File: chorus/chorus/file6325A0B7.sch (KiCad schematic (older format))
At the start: 6 parts, among them U2 TL074

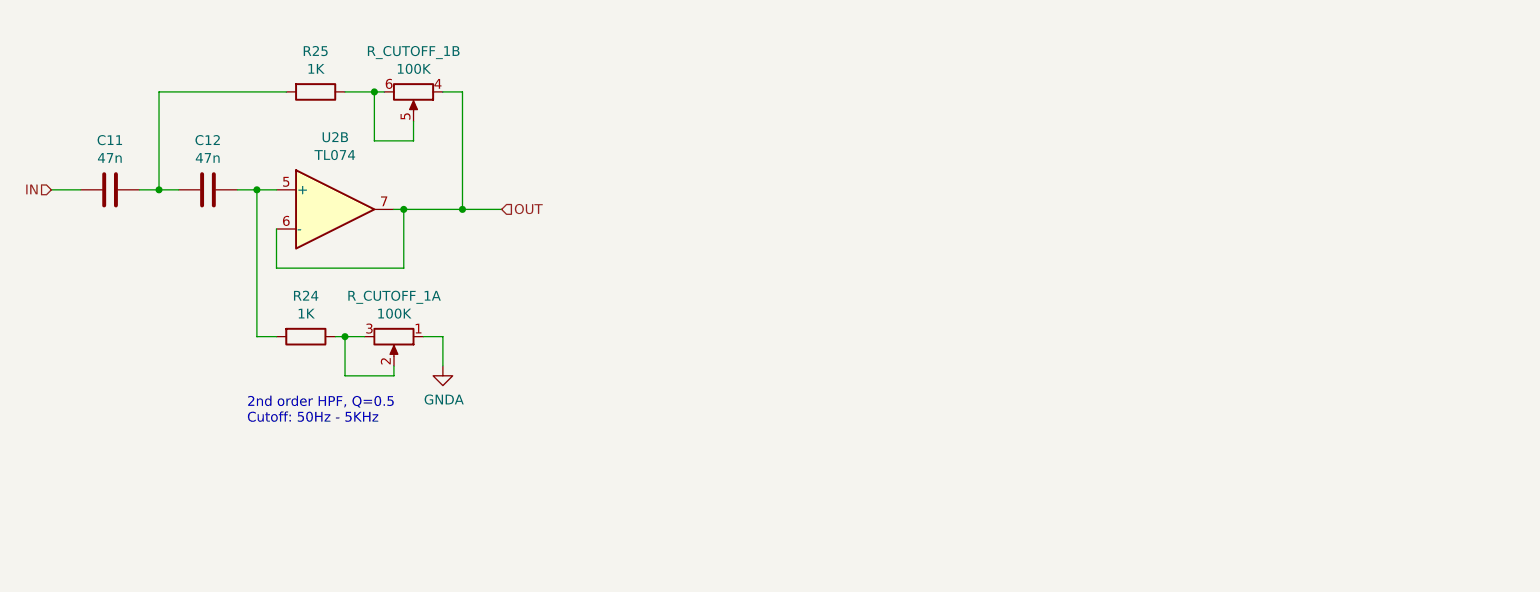
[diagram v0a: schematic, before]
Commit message: add wet/dry mix and recalculate filters
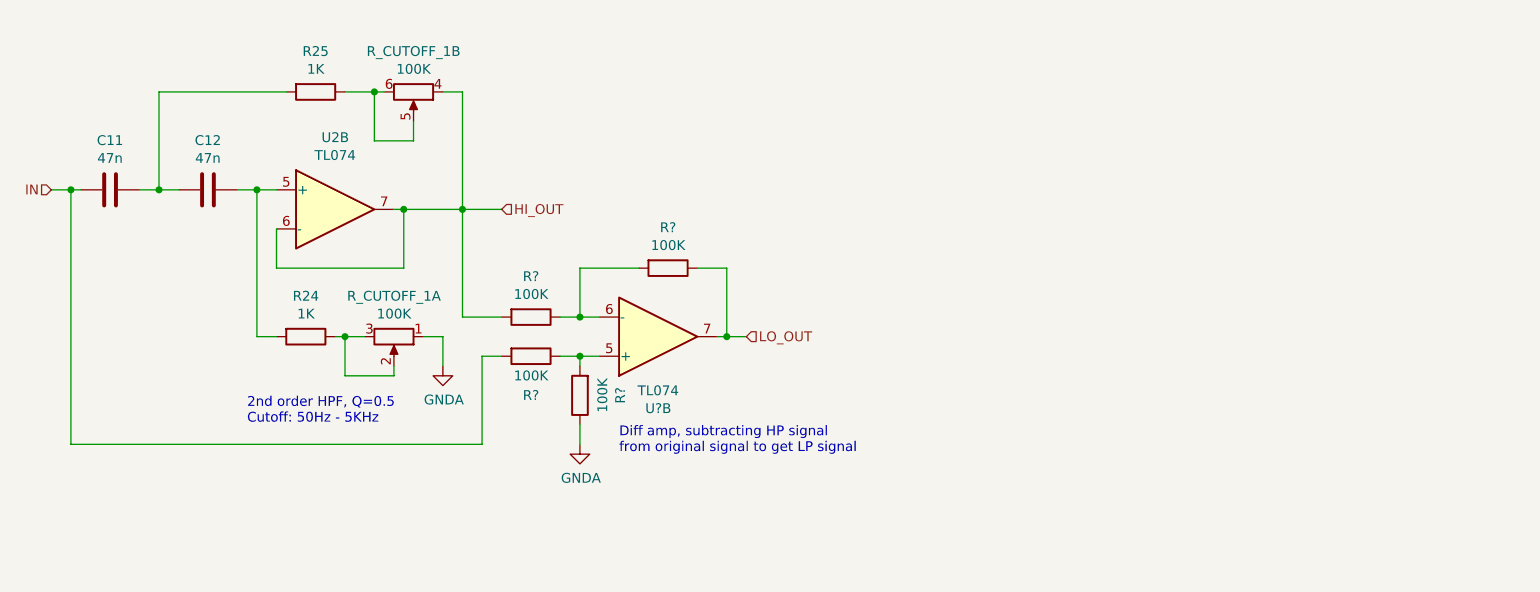
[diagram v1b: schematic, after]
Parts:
- added R? (x4): 100K, Resistor_THT:R_Axial_DIN0204_L3.6mm_D1.6mm_P2.54mm_Vertical, symbol Device:R
- added U?: TL074, Package_DIP:DIP-14_W7.62mm, symbol Amplifier_Operational:TL074
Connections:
- net GNDA: now also R?.1
- net IN: now also R?.2
- net OUT renamed HI_OUT
- net HI_OUT: now also R?.2
- new net: R?.1, R?.2, U?.5 (+)
- new net: R?.1, R?.2, U?.6 (-)
- new net LO_OUT: R?.1, U?.7
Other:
- note added: "Diff amp, subtracting HP signal\nfrom original signal to get LP signal"
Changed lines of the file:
@@
 $Descr A4 11693 8268
 encoding utf-8
-Sheet 6 6
+Sheet 5 6
 Title ""
 Date ""
@@
 IN
 Wire Wire Line
-	4000 3600 4150 3600
+	4000 3600 4100 3600
 Text HLabel 6300 3700 2    50   Input ~ 0
-OUT
+HI_OUT
+Text HLabel 7550 4350 2    50   Input ~ 0
+LO_OUT
+$Comp
+L Amplifier_Operational:TL074 U?
+U 2 1 62A49A72
+P 7100 4350
+AR Path="/62A49A72" Ref="U?"  Part="2"
+AR Path="/6325A0B8/62A49A72" Ref="U?"  Part="2"
+F 0 "U?" H 7100 4717 50  0000 C CNN
+F 1 "TL074" H 7100 4626 50  0000 C CNN
+F 2 "Package_DIP:DIP-14_W7.62mm" H 7050 4450 50  0001 C CNN
+F 3 "http://www.ti.com/lit/ds/symlink/tl071.pdf" H 7150 4550 50  0001 C CNN
+	2    7100 4350
+	1    0    0    1
+$EndComp
+Text Notes 6900 4950 0    50   ~ 0
+Diff amp, subtracting HP signal\nfrom original signal to get LP signal
+$Comp
+L Device:R R?
+U 1 1 62A50D45
+P 6450 4450
+AR Path="/62A50D45" Ref="R?"  Part="1"
+AR Path="/6325A0B8/62A50D45" Ref="R?"  Part="1"
+F 0 "R?" V 6650 4450 50  0000 C CNN
+F 1 "100K" V 6550 4450 50  0000 C CNN
+F 2 "Resistor_THT:R_Axial_DIN0204_L3.6mm_D1.6mm_P2.54mm_Vertical" V 6380 4450 50  0001 C CNN
+F 3 "~" H 6450 4450 50  0001 C CNN
+	1    6450 4450
+	0    1    1    0
+$EndComp
+$Comp
+L Device:R R?
+U 1 1 62A52C2B
+P 6450 4250
+AR Path="/62A52C2B" Ref="R?"  Part="1"
+AR Path="/6325A0B8/62A52C2B" Ref="R?"  Part="1"
+F 0 "R?" V 6243 4250 50  0000 C CNN
+F 1 "100K" V 6334 4250 50  0000 C CNN
+F 2 "Resistor_THT:R_Axial_DIN0204_L3.6mm_D1.6mm_P2.54mm_Vertical" V 6380 4250 50  0001 C CNN
+F 3 "~" H 6450 4250 50  0001 C CNN
+	1    6450 4250
+	0    1    1    0
+$EndComp
+$Comp
+L Device:R R?
+U 1 1 62A53369
+P 7150 4000
+AR Path="/62A53369" Ref="R?"  Part="1"
+AR Path="/6325A0B8/62A53369" Ref="R?"  Part="1"
+F 0 "R?" V 6943 4000 50  0000 C CNN
+F 1 "100K" V 7034 4000 50  0000 C CNN
+F 2 "Resistor_THT:R_Axial_DIN0204_L3.6mm_D1.6mm_P2.54mm_Vertical" V 7080 4000 50  0001 C CNN
+F 3 "~" H 7150 4000 50  0001 C CNN
+	1    7150 4000
+	0    1    1    0
+$EndComp
+$Comp
+L Device:R R?
+U 1 1 62A538EE
+P 6700 4650
+AR Path="/62A538EE" Ref="R?"  Part="1"
+AR Path="/6325A0B8/62A538EE" Ref="R?"  Part="1"
+F 0 "R?" V 6493 4650 50  0000 C CNN
+F 1 "100K" V 6584 4650 50  0000 C CNN
+F 2 "Resistor_THT:R_Axial_DIN0204_L3.6mm_D1.6mm_P2.54mm_Vertical" V 6630 4650 50  0001 C CNN
+F 3 "~" H 6700 4650 50  0001 C CNN
+	1    6700 4650
+	-1   0    0    1
+$EndComp
+Wire Wire Line
+	6600 4450 6700 4450
+Wire Wire Line
+	6700 4500 6700 4450
+Connection ~ 6700 4450
+Wire Wire Line
+	6700 4450 6800 4450
+Wire Wire Line
+	6600 4250 6700 4250
+Wire Wire Line
+	7000 4000 6700 4000
+Wire Wire Line
+	6700 4000 6700 4250
+Connection ~ 6700 4250
+Wire Wire Line
+	6700 4250 6800 4250
+Wire Wire Line
+	7400 4350 7450 4350
+Wire Wire Line
+	7450 4350 7450 4000
+Wire Wire Line
+	7450 4000 7300 4000
+Wire Wire Line
+	7550 4350 7450 4350
+Connection ~ 7450 4350
+$Comp
+L power:GNDA #PWR?
+U 1 1 62A57D82
+P 6700 4900
+AR Path="/62A57D82" Ref="#PWR?"  Part="1"
+AR Path="/6325A0B8/62A57D82" Ref="#PWR?"  Part="1"
+F 0 "#PWR?" H 6700 4650 50  0001 C CNN
+F 1 "GNDA" H 6705 4727 50  0000 C CNN
+F 2 "" H 6700 4900 50  0001 C CNN
+F 3 "" H 6700 4900 50  0001 C CNN
+	1    6700 4900
+	1    0    0    -1
+$EndComp
+Wire Wire Line
+	6700 4900 6700 4800
+Wire Wire Line
+	6300 4450 6200 4450
+Wire Wire Line
+	6200 4450 6200 4900
+Wire Wire Line
+	6200 4900 4100 4900
+Wire Wire Line
+	4100 4900 4100 3600
+Connection ~ 4100 3600
+Wire Wire Line
+	4100 3600 4150 3600
+Wire Wire Line
+	6300 4250 6100 4250
+Wire Wire Line
+	6100 4250 6100 3700
 $EndSCHEMATC

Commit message: remove dry/wet, add higher dry frequencies
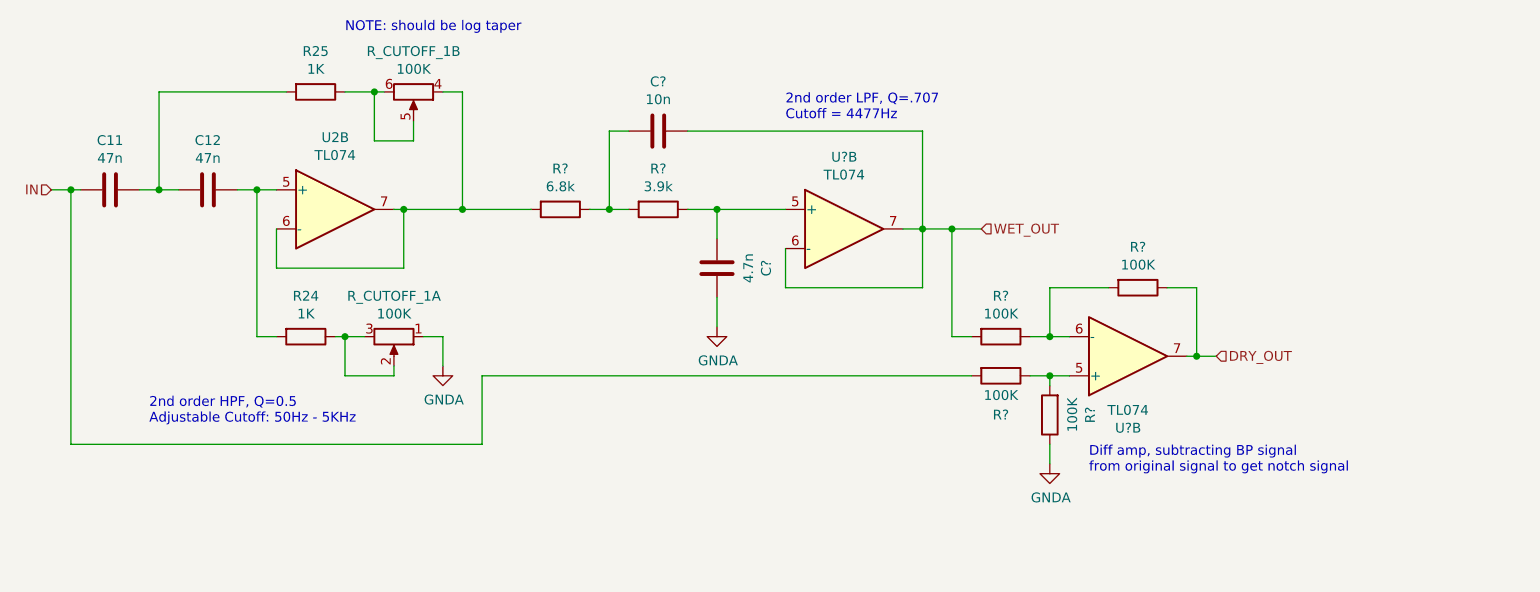
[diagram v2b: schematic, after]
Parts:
- added C?: 10n, Capacitor_THT:C_Disc_D6.0mm_W2.5mm_P5.00mm, symbol Device:C
- added C?: 4.7n, Capacitor_THT:C_Disc_D6.0mm_W2.5mm_P5.00mm, symbol Device:C
- added R?: 6.8k, Resistor_THT:R_Axial_DIN0204_L3.6mm_D1.6mm_P2.54mm_Vertical, symbol Device:R
- added R?: 3.9k, Resistor_THT:R_Axial_DIN0204_L3.6mm_D1.6mm_P2.54mm_Vertical, symbol Device:R
- added U?: TL074, Package_DIP:DIP-14_W7.62mm, symbol Amplifier_Operational:TL074
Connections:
- net GNDA: now also C?.1
- net HI_OUT: no longer names the net of R_CUTOFF_1.4, U2.6 (-), U2.7
- net HI_OUT: now also R?.2; no longer R?.2
- net LO_OUT renamed DRY_OUT
- new net: C?.2, R?.1, U?.5 (+)
- new net: C?.2, R?.1, R?.2
- new net WET_OUT: C?.1, R?.2, U?.6 (-), U?.7
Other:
- note added: "2nd order HPF, Q=0.5\nAdjustable Cutoff: 50Hz - 5KHz"
- note added: "2nd order LPF, Q=.707\nCutoff = 4477Hz"
- note added: "Diff amp, subtracting BP signal\nfrom original signal to get notch signal"
- note added: "NOTE: should be log taper"
- note removed: "2nd order HPF, Q=0.5\nCutoff: 50Hz - 5KHz"
- note removed: "Diff amp, subtracting HP signal\nfrom original signal to get LP signal"
- moved on the sheet: R?, U?B

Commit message: improve BP calculations imperically
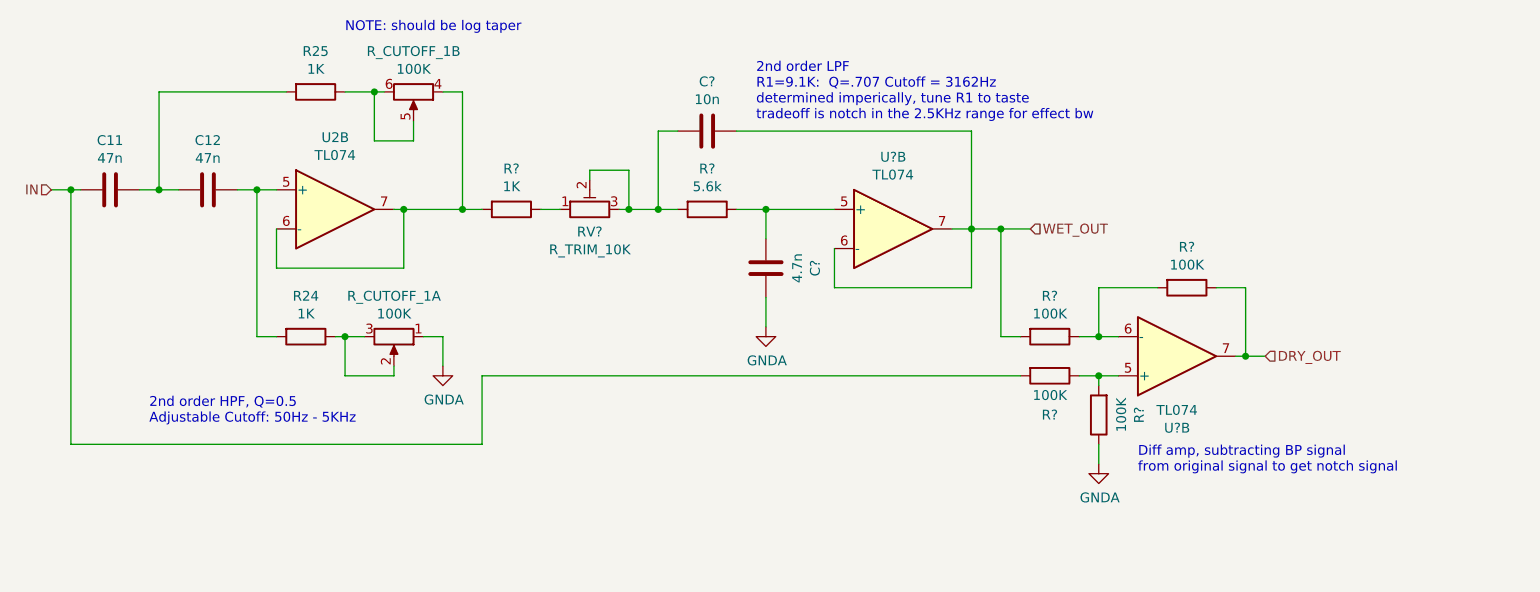
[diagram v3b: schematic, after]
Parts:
- added RV?: R_TRIM_10K, symbol Device:R_POT_TRIM
- R?: value 6.8k -> 1K
- R?: value 3.9k -> 5.6k
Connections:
- net at C?.2, R?.2: now also RV?.2, RV?.3; no longer R?.1
- new net: R?.1, RV?.1
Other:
- note added: "2nd order LPF\nR1=9.1K: Q=.707 Cutoff = 3162Hz\ndetermined imperically, tune R1 to taste\ntradeoff is notch in the 2.5KHz range for effect bw"
- note removed: "2nd order LPF, Q=.707\nCutoff = 4477Hz"
- moved on the sheet: C?, R?, U?B

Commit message: assembled psu and clock
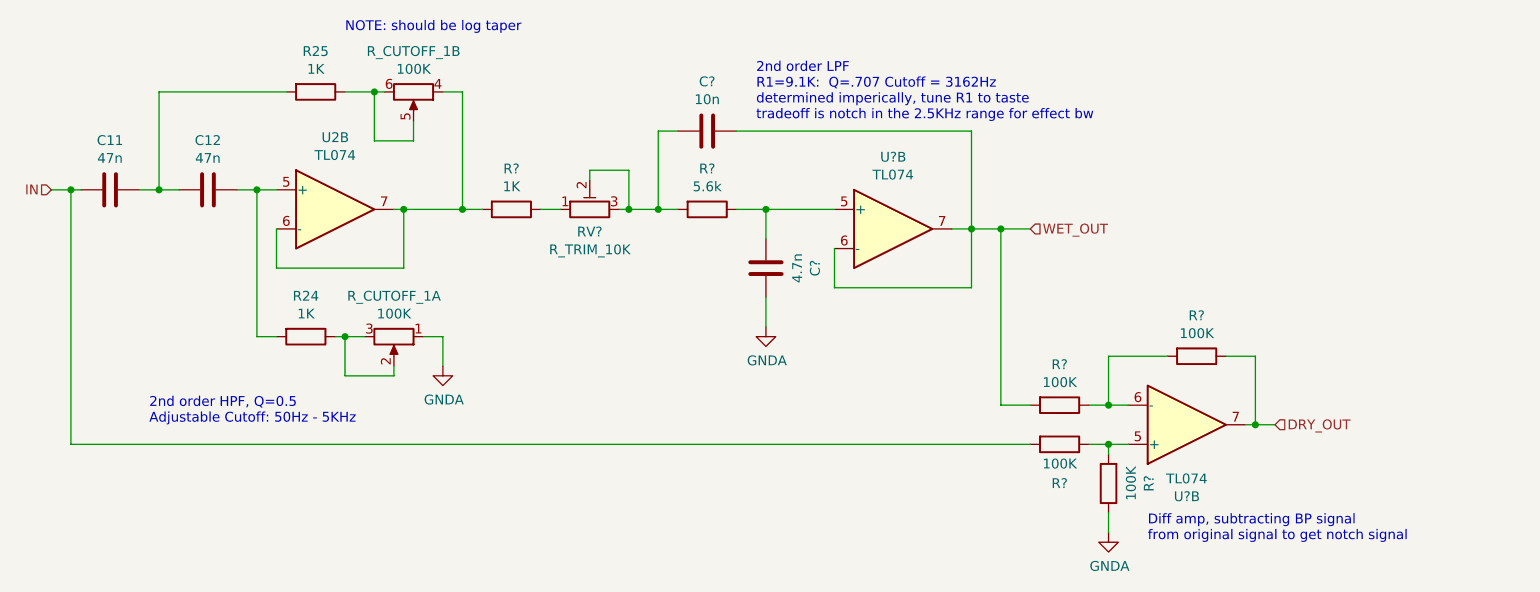
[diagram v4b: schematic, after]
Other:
- moved on the sheet: R?, U?B
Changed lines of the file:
@@
 Text HLabel 9000 3800 2    50   Input ~ 0
 WET_OUT
-Text HLabel 10200 4450 2    50   Input ~ 0
+Text HLabel 10250 4800 2    50   Input ~ 0
 DRY_OUT
 $Comp
 L Amplifier_Operational:TL074 U?
 U 2 1 62A49A72
-P 9750 4450
+P 9800 4800
 AR Path="/62A49A72" Ref="U?"  Part="2"
 AR Path="/6325A0B8/62A49A72" Ref="U?"  Part="2"
-F 0 "U?" H 9750 4817 50  0000 C CNN
-F 1 "TL074" H 9750 4726 50  0000 C CNN
-F 2 "Package_DIP:DIP-14_W7.62mm" H 9700 4550 50  0001 C CNN
-F 3 "http://www.ti.com/lit/ds/symlink/tl071.pdf" H 9800 4650 50  0001 C CNN
-	2    9750 4450
+F 0 "U?" H 9800 5167 50  0000 C CNN
+F 1 "TL074" H 9800 5076 50  0000 C CNN
+F 2 "Package_DIP:DIP-14_W7.62mm" H 9750 4900 50  0001 C CNN
+F 3 "http://www.ti.com/lit/ds/symlink/tl071.pdf" H 9850 5000 50  0001 C CNN
+	2    9800 4800
 	1    0    0    1
 $EndComp
-Text Notes 9550 5050 0    50   ~ 0
+Text Notes 9600 5400 0    50   ~ 0
 Diff amp, subtracting BP signal\nfrom original signal to get notch signal
 $Comp
 L Device:R R?
 U 1 1 62A50D45
-P 9100 4550
+P 9150 4900
 AR Path="/62A50D45" Ref="R?"  Part="1"
 AR Path="/6325A0B8/62A50D45" Ref="R?"  Part="1"
-F 0 "R?" V 9300 4550 50  0000 C CNN
-F 1 "100K" V 9200 4550 50  0000 C CNN
-F 2 "Resistor_THT:R_Axial_DIN0204_L3.6mm_D1.6mm_P2.54mm_Vertical" V 9030 4550 50  0001 C CNN
-F 3 "~" H 9100 4550 50  0001 C CNN
-	1    9100 4550
+F 0 "R?" V 9350 4900 50  0000 C CNN
+F 1 "100K" V 9250 4900 50  0000 C CNN
+F 2 "Resistor_THT:R_Axial_DIN0204_L3.6mm_D1.6mm_P2.54mm_Vertical" V 9080 4900 50  0001 C CNN
+F 3 "~" H 9150 4900 50  0001 C CNN
+	1    9150 4900
 	0    1    1    0
 $EndComp
@@
 L Device:R R?
 U 1 1 62A52C2B
-P 9100 4350
+P 9150 4700
 AR Path="/62A52C2B" Ref="R?"  Part="1"
 AR Path="/6325A0B8/62A52C2B" Ref="R?"  Part="1"
-F 0 "R?" V 8893 4350 50  0000 C CNN
-F 1 "100K" V 8984 4350 50  0000 C CNN
-F 2 "Resistor_THT:R_Axial_DIN0204_L3.6mm_D1.6mm_P2.54mm_Vertical" V 9030 4350 50  0001 C CNN
-F 3 "~" H 9100 4350 50  0001 C CNN
-	1    9100 4350
+F 0 "R?" V 8943 4700 50  0000 C CNN
+F 1 "100K" V 9034 4700 50  0000 C CNN
+F 2 "Resistor_THT:R_Axial_DIN0204_L3.6mm_D1.6mm_P2.54mm_Vertical" V 9080 4700 50  0001 C CNN
+F 3 "~" H 9150 4700 50  0001 C CNN
+	1    9150 4700
 	0    1    1    0
 $EndComp
@@
 L Device:R R?
 U 1 1 62A53369
-P 9800 4100
+P 9850 4450
 AR Path="/62A53369" Ref="R?"  Part="1"
 AR Path="/6325A0B8/62A53369" Ref="R?"  Part="1"
-F 0 "R?" V 9593 4100 50  0000 C CNN
-F 1 "100K" V 9684 4100 50  0000 C CNN
-F 2 "Resistor_THT:R_Axial_DIN0204_L3.6mm_D1.6mm_P2.54mm_Vertical" V 9730 4100 50  0001 C CNN
-F 3 "~" H 9800 4100 50  0001 C CNN
-	1    9800 4100
+F 0 "R?" V 9643 4450 50  0000 C CNN
+F 1 "100K" V 9734 4450 50  0000 C CNN
+F 2 "Resistor_THT:R_Axial_DIN0204_L3.6mm_D1.6mm_P2.54mm_Vertical" V 9780 4450 50  0001 C CNN
+F 3 "~" H 9850 4450 50  0001 C CNN
+	1    9850 4450
 	0    1    1    0
 $EndComp
@@
 L Device:R R?
 U 1 1 62A538EE
-P 9350 4750
+P 9400 5100
 AR Path="/62A538EE" Ref="R?"  Part="1"
 AR Path="/6325A0B8/62A538EE" Ref="R?"  Part="1"
-F 0 "R?" V 9143 4750 50  0000 C CNN
-F 1 "100K" V 9234 4750 50  0000 C CNN
-F 2 "Resistor_THT:R_Axial_DIN0204_L3.6mm_D1.6mm_P2.54mm_Vertical" V 9280 4750 50  0001 C CNN
-F 3 "~" H 9350 4750 50  0001 C CNN
-	1    9350 4750
+F 0 "R?" V 9193 5100 50  0000 C CNN
+F 1 "100K" V 9284 5100 50  0000 C CNN
+F 2 "Resistor_THT:R_Axial_DIN0204_L3.6mm_D1.6mm_P2.54mm_Vertical" V 9330 5100 50  0001 C CNN
+F 3 "~" H 9400 5100 50  0001 C CNN
+	1    9400 5100
 	-1   0    0    1
 $EndComp
 Wire Wire Line
-	9250 4550 9350 4550
-Wire Wire Line
-	9350 4600 9350 4550
-Connection ~ 9350 4550
-Wire Wire Line
-	9350 4550 9450 4550
-Wire Wire Line
-	9250 4350 9350 4350
-Wire Wire Line
-	9650 4100 9350 4100
-Wire Wire Line
-	9350 4100 9350 4350
-Connection ~ 9350 4350
-Wire Wire Line
-	9350 4350 9450 4350
-Wire Wire Line
-	10050 4450 10100 4450
-Wire Wire Line
-	10100 4450 10100 4100
-Wire Wire Line
-	10100 4100 9950 4100
-Wire Wire Line
-	10200 4450 10100 4450
-Connection ~ 10100 4450
+	9300 4900 9400 4900
+Wire Wire Line
+	9400 4950 9400 4900
+Connection ~ 9400 4900
+Wire Wire Line
+	9400 4900 9500 4900
+Wire Wire Line
+	9300 4700 9400 4700
+Wire Wire Line
+	9700 4450 9400 4450
+Wire Wire Line
+	9400 4450 9400 4700
+Connection ~ 9400 4700
+Wire Wire Line
+	9400 4700 9500 4700
+Wire Wire Line
+	10100 4800 10150 4800
+Wire Wire Line
+	10150 4800 10150 4450
+Wire Wire Line
+	10150 4450 10000 4450
+Wire Wire Line
+	10250 4800 10150 4800
+Connection ~ 10150 4800
 $Comp
 L power:GNDA #PWR?
 U 1 1 62A57D82
-P 9350 5000
+P 9400 5350
 AR Path="/62A57D82" Ref="#PWR?"  Part="1"
 AR Path="/6325A0B8/62A57D82" Ref="#PWR?"  Part="1"
-F 0 "#PWR?" H 9350 4750 50  0001 C CNN
-F 1 "GNDA" H 9355 4827 50  0000 C CNN
-F 2 "" H 9350 5000 50  0001 C CNN
-F 3 "" H 9350 5000 50  0001 C CNN
-	1    9350 5000
+F 0 "#PWR?" H 9400 5100 50  0001 C CNN
+F 1 "GNDA" H 9405 5177 50  0000 C CNN
+F 2 "" H 9400 5350 50  0001 C CNN
+F 3 "" H 9400 5350 50  0001 C CNN
+	1    9400 5350
 	1    0    0    -1
 $EndComp
 Wire Wire Line
-	9350 5000 9350 4900
-Wire Wire Line
-	6200 4900 4100 4900
+	9400 5350 9400 5250
 Wire Wire Line
 	4100 4900 4100 3600
@@
 2nd order LPF\nR1=9.1K:  Q=.707 Cutoff = 3162Hz\ndetermined imperically, tune R1 to taste\ntradeoff is notch in the 2.5KHz range for effect bw
 Wire Wire Line
-	8950 4350 8850 4350
-Wire Wire Line
-	8850 4350 8850 3800
-Wire Wire Line
 	8700 3800 8850 3800
 Wire Wire Line
 	8850 3800 9000 3800
 Connection ~ 8850 3800
-Wire Wire Line
-	6200 4550 6200 4900
 $Comp
 L Device:R_POT_TRIM RV?
@@
 Connection ~ 6100 3700
 Wire Wire Line
-	6200 4550 8950 4550
+	4100 4900 9000 4900
+Wire Wire Line
+	9000 4700 8850 4700
+Wire Wire Line
+	8850 3800 8850 4700
 $EndSCHEMATC
